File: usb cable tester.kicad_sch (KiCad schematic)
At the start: 61 parts, among them J1 USB_C_all_pins, J2 USB3_B_Micro, J3 USB3_B, J4 USB3_A, J5 USB_C_all_pins, J6 USB_B_Mini

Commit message: Updated net names to make stuff more understanable
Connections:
- net SBU2_B8: now reaches J5.B8 (SBU2), R21.1
- net VBUS_B9: now reaches J5.B9 (VBUS), R5.1
- net GND_B12: now reaches J5.B12 (GND), R22.1
- net RX2-_A10: now reaches J5.A10 (RX2-), R16.1
- net VBUS_B4: now reaches J5.B4 (VBUS), R4.1
- net D-_A7: now reaches J4.2 (D-), J5.A7 (D-), R8.1
- net D+_B6: now reaches J5.B6 (D+), R11.1
- net TX2-_B3: now reaches J5.B3 (TX2-), R18.1
- net SHIELD: now reaches J4.10 (SHIELD), J5.S1 (SHIELD), R26.1
- net D+_A6: now reaches J4.3 (D+), J5.A6 (D+), R10.1
- net TX2+_B2: now reaches J5.B2 (TX2+), R19.1
- net GND_A1: now reaches J4.4 (GND), J5.A1 (GND), R25.1
- net DRAIN: now reaches J4.7 (DRAIN), R1.1
- net VBUS_A4: now reaches J4.1 (VBUS), J5.A4 (VBUS), R2.1
- net OTG: now reaches J2.4 (ID), J6.4 (ID), R27.1
- net TX1+_A2: now reaches J4.9 (SSTX+), J5.A2 (TX1+), R15.1
- net SBU1_A8: now reaches J5.A8 (SBU1), R20.1
- net RX2+_A11: now reaches J5.A11 (RX2+), R17.1
- net D-_B7: now reaches J5.B7 (D-), R9.1
- net RX1-_B10: now reaches J4.5 (SSRX-), J5.B10 (RX1-), R12.1
- net RX1+_B11: now reaches J4.6 (SSRX+), J5.B11 (RX1+), R13.1
- net TX1-_A3: now reaches J4.8 (SSTX-), J5.A3 (TX1-), R14.1
- net GND_B1: now reaches J5.B1 (GND), R23.1
- net CC1_A5: now reaches J5.A5 (CC1), R6.1
- net GND_A12: now reaches J5.A12 (GND), R24.1
- net VBUS_A9: now reaches J5.A9 (VBUS), R3.1
- net CC2_B5: now reaches J5.B5 (CC2), R7.1
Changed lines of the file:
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@@
+    (effects (font (size 1.27 1.27)) (justify left bottom))
+  )
+  (label "CC2_B5" (at 210.82 82.55 0)
+    (effects (font (size 1.27 1.27)) (justify left bottom))
+  )
+  (label "DRAIN" (at 210.82 58.42 0)
+    (effects (font (size 1.27 1.27)) (justify left bottom))
+  )
+  (label "D-_B7" (at 210.82 90.17 0)
+    (effects (font (size 1.27 1.27)) (justify left bottom))
+  )
+  (label "CC1_A5" (at 210.82 80.01 0)
+    (effects (font (size 1.27 1.27)) (justify left bottom))
+  )
+  (label "GND_B12" (at 210.82 143.51 0)
+    (effects (font (size 1.27 1.27)) (justify left bottom))
+  )
+  (label "SBU1_A8" (at 210.82 130.81 0)
+    (effects (font (size 1.27 1.27)) (justify left bottom))
+  )
+  (label "RX2+_A11" (at 210.82 118.11 0)
+    (effects (font (size 1.27 1.27)) (justify left bottom))
+  )
+  (label "VBUS_A9" (at 210.82 69.85 0)
+    (effects (font (size 1.27 1.27)) (justify left bottom))
+  )
+  (label "VBUS_A4" (at 210.82 67.31 0)
+    (effects (font (size 1.27 1.27)) (justify left bottom))
+  )
+  (label "TX1+_A2" (at 210.82 110.49 0)
+    (effects (font (size 1.27 1.27)) (justify left bottom))
+  )
+  (label "D+_B6" (at 210.82 95.25 0)
+    (effects (font (size 1.27 1.27)) (justify left bottom))
+  )
+  (label "OTG" (at 85.09 35.56 0)
+    (effects (font (size 1.27 1.27)) (justify left bottom))
+  )
+  (label "RX1+_B11" (at 210.82 102.87 0)
+    (effects (font (size 1.27 1.27)) (justify left bottom))
+  )
+  (label "SHIELD" (at 210.82 156.21 0)
+    (effects (font (size 1.27 1.27)) (justify left bottom))
+  )
+  (label "GND_A1" (at 210.82 151.13 0)
+    (effects (font (size 1.27 1.27)) (justify left bottom))
+  )
+  (label "D+_A6" (at 210.82 92.71 0)
+    (effects (font (size 1.27 1.27)) (justify left bottom))
+  )
+  (label "TX2+_B2" (at 210.82 125.73 0)
+    (effects (font (size 1.27 1.27)) (justify left bottom))
+  )
+  (label "VBUS_B9" (at 210.82 74.93 0)
+    (effects (font (size 1.27 1.27)) (justify left bottom))
+  )
+  (label "RX2-_A10" (at 210.82 115.57 0)
+    (effects (font (size 1.27 1.27)) (justify left bottom))
+  )
+  (label "TX1-_A3" (at 210.82 107.95 0)
+    (effects (font (size 1.27 1.27)) (justify left bottom))
+  )
+  (label "D-_A7" (at 210.82 87.63 0)
+    (effects (font (size 1.27 1.27)) (justify left bottom))
+  )
+  (label "SBU2_B8" (at 210.82 133.35 0)
+    (effects (font (size 1.27 1.27)) (justify left bottom))
+  )
+  (label "VBUS_B4" (at 210.82 72.39 0)
+    (effects (font (size 1.27 1.27)) (justify left bottom))
+  )
+  (label "GND_A12" (at 210.82 148.59 0)
+    (effects (font (size 1.27 1.27)) (justify left bottom))
+  )
+  (label "TX2-_B3" (at 210.82 123.19 0)
+    (effects (font (size 1.27 1.27)) (justify left bottom))
+  )
+  (label "RX1-_B10" (at 210.82 100.33 0)
+    (effects (font (size 1.27 1.27)) (justify left bottom))
+  )
+  (label "GND_B1" (at 210.82 146.05 0)
     (effects (font (size 1.27 1.27)) (justify left bottom))
   )

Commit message: Synced footprints and changed references
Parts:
- BT1: footprint misc:BATT MY-2032-16 -> misc:BATT CR2032
- J1, J5: footprint misc:USB-C Molex 105450 -> misc:USB-C
- J2: footprint misc:USB3_Micro-AB -> misc:USB Micro-AB 3.0
- J3: footprint misc:USB 3.0 B -> misc:USB-B 3.0
- J4: footprint misc:USB 3.0 A XKB U231-091N-4BLRA00-S -> misc:USB-A 3.0
- J6: footprint misc:USB Mini-AB - Molex 565790576 -> misc:USB Mini-AB
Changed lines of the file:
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@@
     (property "Reference" "J2" (id 0) (at 64.77 16.51 0))
     (property "Value" "USB3_B_Micro" (id 1) (at 64.77 19.05 0))
-    (property "Footprint" "misc:USB3_Micro-AB" (id 2) (at 68.58 31.75 0)
+    (property "Footprint" "misc:USB Micro-AB 3.0" (id 2) (at 68.58 31.75 0)
       (effects (font (size 1.27 1.27)) hide)
     )
@@
     (property "Reference" "J4" (id 0) (at 191.77 19.05 0))
     (property "Value" "USB3_A" (id 1) (at 191.77 21.59 0))
-    (property "Footprint" "misc:USB 3.0 A XKB U231-091N-4BLRA00-S" (id 2) (at 195.58 35.56 0)
+    (property "Footprint" "misc:USB-A 3.0" (id 2) (at 195.58 35.56 0)
       (effects (font (size 1.27 1.27)) hide)
     )
@@
     (property "Reference" "J3" (id 0) (at 64.77 59.69 0))
     (property "Value" "USB3_B" (id 1) (at 64.77 62.23 0))
-    (property "Footprint" "misc:USB 3.0 B" (id 2) (at 68.58 76.2 0)
+    (property "Footprint" "misc:USB-B 3.0" (id 2) (at 68.58 76.2 0)
       (effects (font (size 1.27 1.27)) hide)
     )
@@
     (property "Reference" "J6" (id 0) (at 92.71 35.56 0))
     (property "Value" "USB_B_Mini" (id 1) (at 92.71 38.1 0))
-    (property "Footprint" "misc:USB Mini-AB - Molex 565790576" (id 2) (at 96.52 49.53 0)
+    (property "Footprint" "misc:USB Mini-AB" (id 2) (at 96.52 49.53 0)
       (effects (font (size 1.27 1.27)) hide)
     )
@@
     (property "Reference" "J1" (id 0) (at 29.21 16.51 0))
     (property "Value" "USB_C_all_pins" (id 1) (at 29.21 19.05 0))
-    (property "Footprint" "misc:USB-C Molex 105450" (id 2) (at 34.29 54.61 0)
+    (property "Footprint" "misc:USB-C" (id 2) (at 34.29 54.61 0)
       (effects (font (size 1.27 1.27)) hide)
     )
@@
     (property "Reference" "J5" (id 0) (at 190.5 59.69 0))
     (property "Value" "USB_C_all_pins" (id 1) (at 190.5 62.23 0))
-    (property "Footprint" "misc:USB-C Molex 105450" (id 2) (at 195.58 97.79 0)
+    (property "Footprint" "misc:USB-C" (id 2) (at 195.58 97.79 0)
       (effects (font (size 1.27 1.27)) hide)
     )
@@
       (effects (font (size 1.27 1.27)) (justify left))
     )
-    (property "Footprint" "misc:BATT MY-2032-16" (id 2) (at 25.4 120.396 90)
+    (property "Footprint" "misc:BATT CR2032" (id 2) (at 25.4 120.396 90)
       (effects (font (size 1.27 1.27)) hide)
     )
@@
     )
     (path "/f3bec2e0-eab6-4e3e-9f35-7474b83a7c41"
-      (reference "BT1") (unit 1) (value "Battery_Cell") (footprint "misc:BATT MY-2032-16")
+      (reference "BT1") (unit 1) (value "Battery_Cell") (footprint "misc:BATT CR2032")
     )
     (path "/bdcb84da-7970-44d1-882d-7f6869ae2130"
@@
     )
     (path "/caec39a5-c3f7-4bd2-bf1c-1fbeb1c52454"
-      (reference "J1") (unit 1) (value "USB_C_all_pins") (footprint "misc:USB-C Molex 105450")
+      (reference "J1") (unit 1) (value "USB_C_all_pins") (footprint "misc:USB-C")
     )
     (path "/7089e2ba-2f13-49e0-8b7a-27c0192babf1"
-      (reference "J2") (unit 1) (value "USB3_B_Micro") (footprint "misc:USB3_Micro-AB")
+      (reference "J2") (unit 1) (value "USB3_B_Micro") (footprint "misc:USB Micro-AB 3.0")
     )
     (path "/89fb9d4c-31e7-4cdd-b7ba-6f942631941f"
-      (reference "J3") (unit 1) (value "USB3_B") (footprint "misc:USB 3.0 B")
+      (reference "J3") (unit 1) (value "USB3_B") (footprint "misc:USB-B 3.0")
     )
     (path "/80e86de5-2af9-433b-a1df-f8ebccd25507"
-      (reference "J4") (unit 1) (value "USB3_A") (footprint "misc:USB 3.0 A XKB U231-091N-4BLRA00-S")
+      (reference "J4") (unit 1) (value "USB3_A") (footprint "misc:USB-A 3.0")
     )
     (path "/ed976a99-8e28-49b2-9198-23aae6973f1a"
-      (reference "J5") (unit 1) (value "USB_C_all_pins") (footprint "misc:USB-C Molex 105450")
+      (reference "J5") (unit 1) (value "USB_C_all_pins") (footprint "misc:USB-C")
     )
     (path "/b8ad2479-4df9-41d1-990d-e989122363ae"
-      (reference "J6") (unit 1) (value "USB_B_Mini") (footprint "misc:USB Mini-AB - Molex 565790576")
+      (reference "J6") (unit 1) (value "USB_B_Mini") (footprint "misc:USB Mini-AB")
     )
     (path "/68333741-3656-4504-9969-73b54fe56fb9"

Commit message: Change values of resistors and LEDs
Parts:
- D1: value DRAIN -> Red
- D10, D11: value D+ -> Red
- D12: value RX1- -> Red
- D13: value RX1+ -> Red
- D14: value TX1- -> Red
- D15: value TX1+ -> Red
- D16: value RX2- -> Red
- D17: value RX2+ -> Red
- D18: value TX2- -> Red
- D19: value TX2+ -> Red
- D2, D3, D4, D5: value VBUS -> Red
- D20: value SBU1 -> Red
- D21: value SBU2 -> Red
- D27: value OTG -> Red
- D6: value CC1 -> Red
- D7: value CC2 -> Red
- D8, D9: value D- -> Red
- R1, R10, R11, R12, R13, R14, R15, R16, R17, R18, R19, R2, R20, R21, R27, R3, R4, R5, R6, R7, R8, R9: value 470R -> 1k

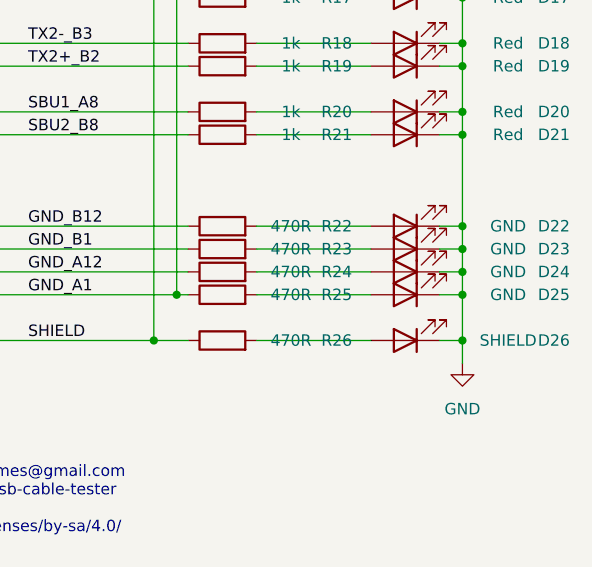
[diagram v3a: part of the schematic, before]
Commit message: Fix values missed before, hide some stuff from BOM
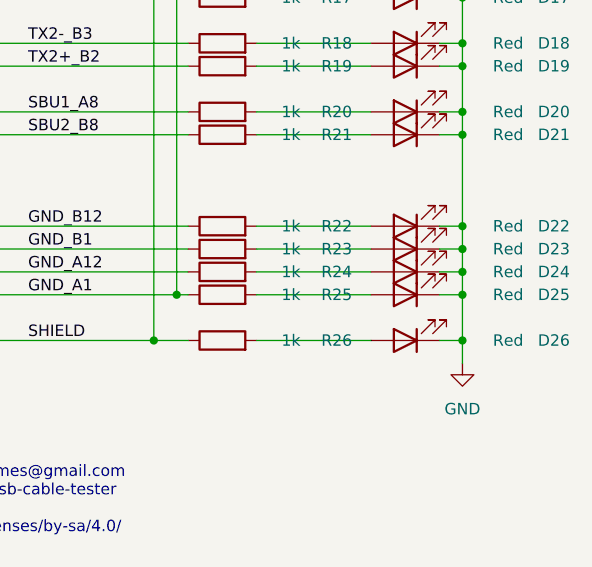
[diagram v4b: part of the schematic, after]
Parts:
- D22, D23, D24, D25: value GND -> Red
- D26: value SHIELD -> Red
- R22, R23, R24, R25, R26: value 470R -> 1k
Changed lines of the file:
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@@
     (in_bom yes) (on_board yes)
     (property "Reference" "D24" (id 0) (at 269.24 148.59 0))
-    (property "Value" "GND" (id 1) (at 264.16 148.59 0))
+    (property "Value" "Red" (id 1) (at 264.16 148.59 0))
     (property "Footprint" "LED_SMD:LED_0805_2012Metric" (id 2) (at 252.73 148.59 0)
       (effects (font (size 1.27 1.27)) hide)
@@
     (in_bom yes) (on_board yes)
     (property "Reference" "R22" (id 0) (at 245.11 143.51 90))
-    (property "Value" "470R" (id 1) (at 240.03 143.51 90))
+    (property "Value" "1k" (id 1) (at 240.03 143.51 90))
     (property "Footprint" "Resistor_SMD:R_0805_2012Metric" (id 2) (at 232.41 145.288 90)
       (effects (font (size 1.27 1.27)) hide)
@@
     (in_bom yes) (on_board yes)
     (property "Reference" "D25" (id 0) (at 269.24 151.13 0))
-    (property "Value" "GND" (id 1) (at 264.16 151.13 0))
+    (property "Value" "Red" (id 1) (at 264.16 151.13 0))
     (property "Footprint" "LED_SMD:LED_0805_2012Metric" (id 2) (at 252.73 151.13 0)
       (effects (font (size 1.27 1.27)) hide)
@@
     (in_bom yes) (on_board yes)
     (property "Reference" "R26" (id 0) (at 245.11 156.21 90))
-    (property "Value" "470R" (id 1) (at 240.03 156.21 90))
+    (property "Value" "1k" (id 1) (at 240.03 156.21 90))
     (property "Footprint" "Resistor_SMD:R_0805_2012Metric" (id 2) (at 232.41 157.988 90)
       (effects (font (size 1.27 1.27)) hide)
@@
     (in_bom yes) (on_board yes)
     (property "Reference" "R25" (id 0) (at 245.11 151.13 90))
-    (property "Value" "470R" (id 1) (at 240.03 151.13 90))
+    (property "Value" "1k" (id 1) (at 240.03 151.13 90))
     (property "Footprint" "Resistor_SMD:R_0805_2012Metric" (id 2) (at 232.41 152.908 90)
       (effects (font (size 1.27 1.27)) hide)
@@
     (in_bom yes) (on_board yes)
     (property "Reference" "R23" (id 0) (at 245.11 146.05 90))
-    (property "Value" "470R" (id 1) (at 240.03 146.05 90))
+    (property "Value" "1k" (id 1) (at 240.03 146.05 90))
     (property "Footprint" "Resistor_SMD:R_0805_2012Metric" (id 2) (at 232.41 147.828 90)
       (effects (font (size 1.27 1.27)) hide)
@@
     (in_bom yes) (on_board yes)
     (property "Reference" "D22" (id 0) (at 269.24 143.51 0))
-    (property "Value" "GND" (id 1) (at 264.16 143.51 0))
+    (property "Value" "Red" (id 1) (at 264.16 143.51 0))
     (property "Footprint" "LED_SMD:LED_0805_2012Metric" (id 2) (at 252.73 143.51 0)
       (effects (font (size 1.27 1.27)) hide)
@@
     (in_bom yes) (on_board yes)
     (property "Reference" "D23" (id 0) (at 269.24 146.05 0))
-    (property "Value" "GND" (id 1) (at 264.16 146.05 0))
+    (property "Value" "Red" (id 1) (at 264.16 146.05 0))
     (property "Footprint" "LED_SMD:LED_0805_2012Metric" (id 2) (at 252.73 146.05 0)
       (effects (font (size 1.27 1.27)) hide)
@@
     (in_bom yes) (on_board yes)
     (property "Reference" "R24" (id 0) (at 245.11 148.59 90))
-    (property "Value" "470R" (id 1) (at 240.03 148.59 90))
+    (property "Value" "1k" (id 1) (at 240.03 148.59 90))
     (property "Footprint" "Resistor_SMD:R_0805_2012Metric" (id 2) (at 232.41 150.368 90)
       (effects (font (size 1.27 1.27)) hide)
@@
     (in_bom yes) (on_board yes)
     (property "Reference" "D26" (id 0) (at 269.24 156.21 0))
-    (property "Value" "SHIELD" (id 1) (at 264.16 156.21 0))
+    (property "Value" "Red" (id 1) (at 264.16 156.21 0))
     (property "Footprint" "LED_SMD:LED_0805_2012Metric" (id 2) (at 252.73 156.21 0)
       (effects (font (size 1.27 1.27)) hide)
@@
     )
     (path "/84df821b-49f2-4e4b-bba8-f4b41cee33b5"
-      (reference "D22") (unit 1) (value "GND") (footprint "LED_SMD:LED_0805_2012Metric")
+      (reference "D22") (unit 1) (value "Red") (footprint "LED_SMD:LED_0805_2012Metric")
     )
     (path "/b740ae9c-448d-4142-bd74-75729a331469"
-      (reference "D23") (unit 1) (value "GND") (footprint "LED_SMD:LED_0805_2012Metric")
+      (reference "D23") (unit 1) (value "Red") (footprint "LED_SMD:LED_0805_2012Metric")
     )
     (path "/0959140d-f16b-4730-a211-dbdbb8969383"
-      (reference "D24") (unit 1) (value "GND") (footprint "LED_SMD:LED_0805_2012Metric")
+      (reference "D24") (unit 1) (value "Red") (footprint "LED_SMD:LED_0805_2012Metric")
     )
     (path "/16f06e44-8422-409a-8b33-c44eb20e1a89"
-      (reference "D25") (unit 1) (value "GND") (footprint "LED_SMD:LED_0805_2012Metric")
+      (reference "D25") (unit 1) (value "Red") (footprint "LED_SMD:LED_0805_2012Metric")
     )
     (path "/ee01c69a-da4f-4a7b-89b0-ca4ee1dbc0e5"
-      (reference "D26") (unit 1) (value "SHIELD") (footprint "LED_SMD:LED_0805_2012Metric")
+      (reference "D26") (unit 1) (value "Red") (footprint "LED_SMD:LED_0805_2012Metric")
     )
     (path "/b260f1df-839f-4c6f-af07-b7ac85840c59"
@@
     )
     (path "/159ce2c6-26c9-44fe-8f44-48417cde10c8"
-      (reference "R22") (unit 1) (value "470R") (footprint "Resistor_SMD:R_0805_2012Metric")
+      (reference "R22") (unit 1) (value "1k") (footprint "Resistor_SMD:R_0805_2012Metric")
     )
     (path "/849cb898-ee55-47ce-b8d5-0cff351f8742"
-      (reference "R23") (unit 1) (value "470R") (footprint "Resistor_SMD:R_0805_2012Metric")
+      (reference "R23") (unit 1) (value "1k") (footprint "Resistor_SMD:R_0805_2012Metric")
     )
     (path "/e0c59ceb-47ea-40ff-8ae9-8fe3efd9bf3c"
-      (reference "R24") (unit 1) (value "470R") (footprint "Resistor_SMD:R_0805_2012Metric")
+      (reference "R24") (unit 1) (value "1k") (footprint "Resistor_SMD:R_0805_2012Metric")
     )
     (path "/6118b8cc-b0d1-45c5-a9ce-c83dae98e9ac"
-      (reference "R25") (unit 1) (value "470R") (footprint "Resistor_SMD:R_0805_2012Metric")
+      (reference "R25") (unit 1) (value "1k") (footprint "Resistor_SMD:R_0805_2012Metric")
     )
     (path "/3200205d-5cfc-49f8-8a97-1cbc990ff983"
-      (reference "R26") (unit 1) (value "470R") (footprint "Resistor_SMD:R_0805_2012Metric")
+      (reference "R26") (unit 1) (value "1k") (footprint "Resistor_SMD:R_0805_2012Metric")
     )
     (path "/e1c1b2c5-5b64-4899-920d-c4f93885c402"

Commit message: Added LCSC part numbers
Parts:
- BT1: MPN (none) -> C2902340
- D1: MPN (none) -> C965812
- J1, J5: MPN (none) -> C134092; Source https://www.lcsc.com/product-detail/USB-Connectors_MOLEX-10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 -> (none)
- J2: MPN (none) -> C464578
- J3: MPN (none) -> C2895032
- J4: MPN (none) -> C381140
- J6: MPN (none) -> C505287
- R1: MPN (none) -> C2907295
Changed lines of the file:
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@@
+      (effects (font (size 1.27 1.27)) hide)
+    )
+    (property "MPN" "C2907295" (id 4) (at 232.41 58.42 90)
       (effects (font (size 1.27 1.27)) hide)
     )
@@
       (effects (font (size 1.27 1.27)) hide)
     )
-    (property "Datasheet" "~" (id 3) (at 68.58 30.48 0)
+    (property "Datasheet" "https://datasheet.lcsc.com/lcsc/1912111608_Amphenol-ICC-GSB343133HR_C464578.pdf" (id 3) (at 68.58 30.48 0)
+      (effects (font (size 1.27 1.27)) hide)
+    )
+    (property "MPN" "C464578" (id 4) (at 64.77 35.56 0)
       (effects (font (size 1.27 1.27)) hide)
     )
@@
       (effects (font (size 1.27 1.27)) hide)
     )
-    (property "Datasheet" "~" (id 3) (at 195.58 35.56 0)
+    (property "Datasheet" "https://datasheet.lcsc.com/lcsc/2208041700_XKB-Connectivity-U231-091N-4BLRA00-S-1_C381140.pdf" (id 3) (at 195.58 35.56 0)
+      (effects (font (size 1.27 1.27)) hide)
+    )
+    (property "MPN" "C381140" (id 4) (at 191.77 38.1 0)
       (effects (font (size 1.27 1.27)) hide)
     )
@@
       (effects (font (size 1.27 1.27)) hide)
     )
-    (property "Datasheet" "~" (id 3) (at 68.58 76.2 0)
+    (property "Datasheet" "https://datasheet.lcsc.com/lcsc/2109081830_XUNPU-USB-306BWD-ARW_C2895032.pdf" (id 3) (at 68.58 76.2 0)
+      (effects (font (size 1.27 1.27)) hide)
+    )
+    (property "MPN" "C2895032" (id 4) (at 64.77 78.74 0)
       (effects (font (size 1.27 1.27)) hide)
     )
@@
       (effects (font (size 1.27 1.27)) hide)
     )
-    (property "Datasheet" "~" (id 3) (at 96.52 49.53 0)
+    (property "Datasheet" "https://datasheet.lcsc.com/lcsc/2109161730_MOLEX-565790576_C505287.pdf" (id 3) (at 96.52 49.53 0)
+      (effects (font (size 1.27 1.27)) hide)
+    )
+    (property "MPN" "C505287" (id 4) (at 92.71 48.26 0)
       (effects (font (size 1.27 1.27)) hide)
     )
@@
       (effects (font (size 1.27 1.27)) hide)
     )
+    (property "MPN" "C965812" (id 4) (at 252.73 58.42 0)
+      (effects (font (size 1.27 1.27)) hide)
+    )
     (pin "1")
     (pin "2")
@@
       (effects (font (size 1.27 1.27)) hide)
     )
-    (property "Datasheet" "https://www.usb.org/sites/default/files/documents/usb_type-c.zip" (id 3) (at 34.29 54.61 0)
-      (effects (font (size 1.27 1.27)) hide)
-    )
-    (property "Source" "https://www.lcsc.com/product-detail/USB-Connectors_MOLEX-1054500101_C134092.html" (id 4) (at 30.48 54.61 0)
+    (property "Datasheet" "https://datasheet.lcsc.com/lcsc/1811131824_MOLEX-1054500101_C134092.pdf" (id 3) (at 34.29 54.61 0)
+      (effects (font (size 1.27 1.27)) hide)
+    )
+    (property "MPN" "C134092" (id 4) (at 30.48 54.61 0)
       (effects (font (size 1.27 1.27)) hide)
     )
@@
       (effects (font (size 1.27 1.27)) hide)
     )
-    (property "Datasheet" "https://www.usb.org/sites/default/files/documents/usb_type-c.zip" (id 3) (at 195.58 97.79 0)
-      (effects (font (size 1.27 1.27)) hide)
-    )
-    (property "Source" "https://www.lcsc.com/product-detail/USB-Connectors_MOLEX-1054500101_C134092.html" (id 4) (at 191.77 97.79 0)
+    (property "Datasheet" "https://datasheet.lcsc.com/lcsc/1811131824_MOLEX-1054500101_C134092.pdf" (id 3) (at 195.58 97.79 0)
+      (effects (font (size 1.27 1.27)) hide)
+    )
+    (property "MPN" "C134092" (id 5) (at 191.77 97.79 0)
       (effects (font (size 1.27 1.27)) hide)
     )
@@
       (effects (font (size 1.27 1.27)) hide)
     )
-    (property "Datasheet" "~" (id 3) (at 25.4 120.396 90)
-      (effects (font (size 1.27 1.27)) hide)
-    )
+    (property "Datasheet" "https://datasheet.lcsc.com/lcsc/2109301830_MYOUNG-MY-2032-16_C2902340.pdf" (id 3) (at 25.4 120.396 90)
+      (effects (font (size 1.27 1.27)) hide)
+    )
+    (property "MPN" "C2902340" (id 4) (at 25.4 121.92 0)
+      (effects (font (size 1.27 1.27)) hide)
+    )
